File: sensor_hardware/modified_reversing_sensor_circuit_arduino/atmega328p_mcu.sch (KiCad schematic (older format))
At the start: 15 parts, among them Q1 8/16/20MHz

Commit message: mods to schematic
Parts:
- added R12, R18, R21, R24, R28: R, symbol R
- added U4: LM339, symbol LM339
- gave numbers to parts that had none: 9
- renumbered C2 to C6, C1 to C7, R2 to R32, R6 to R33, Q1 to X1
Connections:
- wire segments 59 -> 73
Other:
- note added: "Atmega328p comparator \nequivalent circuit"
- note added: "comparator electrical characteristics\ninput offset voltage @ 5V \n(conditions 0.4V < Vin <Vcc-0.5V)\n typical 10 mV, max 40 mV\ninput leakage current \n min -50 nA max 50 nA\npropogation delay\n 500 ns"

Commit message: mods to schematic
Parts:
- U1: symbol atmega328p -> atmega328p-RESCUE-reversing_sensor_circuit
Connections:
- net labels added: PosFeedback
- net labels removed: SoftCompOut
- wire segments 73 -> 71
- no-connect marks 0 -> 1
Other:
- note added: "Atmega328 only has \ninternal comp output"
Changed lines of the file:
@@
 EESchema Schematic File Version 2
+LIBS:reversing_sensor_circuit-rescue
 LIBS:power
 LIBS:device
@@
 $EndDescr
 $Comp
-L atmega328p U1
+L atmega328p-RESCUE-reversing_sensor_circuit U1
 U 1 1 61408799
 P 5650 3675
+AR Path="/61408799" Ref="U1"  Part="1"
+AR Path="/61407FAF/61408799" Ref="U1"  Part="1"
 F 0 "U1" H 5650 3375 60  0000 C CNN
 F 1 "atmega328p" H 5350 3025 60  0000 C CNN
@@
 $EndComp
 Text Label 7575 3975 2    60   ~ 0
-SoftCompOut
+PosFeedback
 $Comp
 L R R13
@@
 	8400 950  8575 950
 Connection ~ 8400 1525
-Wire Wire Line
-	9450 1625 9700 1625
-Wire Wire Line
-	9650 1625 9650 950
-Wire Wire Line
-	9650 950  8875 950
 Text Notes 8200 3550 0    60   ~ 0
 comparator electrical characteristics\ninput offset voltage @ 5V \n(conditions 0.4V < Vin <Vcc-0.5V)\n   typical 10 mV, max 40 mV\ninput leakage current           \n   min -50 nA max 50 nA\npropogation delay\n   500 ns
@@
 Wire Wire Line
 	7775 1725 7625 1725
-Text Label 9700 1625 0    60   ~ 0
-SoftCompOut
-Connection ~ 9650 1625
 Text Notes 9175 2175 0    60   ~ 0
 Atmega328p comparator \nequivalent circuit
@@
 Wire Wire Line
 	9050 1325 9050 1225
+Text Label 9100 950  0    60   ~ 0
+PosFeedback
+Wire Wire Line
+	8875 950  9100 950
+NoConn ~ 9450 1625
+Text Notes 9650 1625 0    60   ~ 0
+Atmega328 only has \ninternal comp output
 $EndSCHEMATC

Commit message: internal comparator option1, with a feedback on the positive input, but not tested yet
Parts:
- R12, R21: value R -> 8K2
- R13, R24, R25, R28: value R -> 100K
- R18, R29: value R -> 10K
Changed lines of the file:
@@
 P 8775 4075
 F 0 "R29" V 8855 4075 50  0000 C CNN
-F 1 "R" V 8775 4075 50  0000 C CNN
+F 1 "10K" V 8775 4075 50  0000 C CNN
 F 2 "" V 8705 4075 50  0001 C CNN
 F 3 "" H 8775 4075 50  0001 C CNN
@@
 P 8375 4500
 F 0 "R25" V 8455 4500 50  0000 C CNN
-F 1 "R" V 8375 4500 50  0000 C CNN
+F 1 "100K" V 8375 4500 50  0000 C CNN
 F 2 "" V 8305 4500 50  0001 C CNN
 F 3 "" H 8375 4500 50  0001 C CNN
@@
 P 7850 3975
 F 0 "R13" V 7775 3975 50  0000 C CNN
-F 1 "R" V 7850 3975 50  0000 C CNN
+F 1 "100K" V 7850 3975 50  0000 C CNN
 F 2 "" V 7780 3975 50  0001 C CNN
 F 3 "" H 7850 3975 50  0001 C CNN
@@
 P 7925 1525
 F 0 "R18" V 8005 1525 50  0000 C CNN
-F 1 "R" V 7925 1525 50  0000 C CNN
+F 1 "10K" V 7925 1525 50  0000 C CNN
 F 2 "" V 7855 1525 50  0001 C CNN
 F 3 "" H 7925 1525 50  0001 C CNN
@@
 P 8250 2025
 F 0 "R24" V 8330 2025 50  0000 C CNN
-F 1 "R" V 8250 2025 50  0000 C CNN
+F 1 "100K" V 8250 2025 50  0000 C CNN
 F 2 "" V 8180 2025 50  0001 C CNN
 F 3 "" H 8250 2025 50  0001 C CNN
@@
 P 8725 950
 F 0 "R28" V 8805 950 50  0000 C CNN
-F 1 "R" V 8725 950 50  0000 C CNN
+F 1 "100K" V 8725 950 50  0000 C CNN
 F 2 "" V 8655 950 50  0001 C CNN
 F 3 "" H 8725 950 50  0001 C CNN
@@
 P 7350 4175
 F 0 "R12" V 7430 4175 50  0000 C CNN
-F 1 "R" V 7350 4175 50  0000 C CNN
+F 1 "8K2" V 7350 4175 50  0000 C CNN
 F 2 "" V 7280 4175 50  0001 C CNN
 F 3 "" H 7350 4175 50  0001 C CNN
@@
 P 7925 1725
 F 0 "R21" V 8005 1725 50  0000 C CNN
-F 1 "R" V 7925 1725 50  0000 C CNN
+F 1 "8K2" V 7925 1725 50  0000 C CNN
 F 2 "" V 7855 1725 50  0001 C CNN
 F 3 "" H 7925 1725 50  0001 C CNN

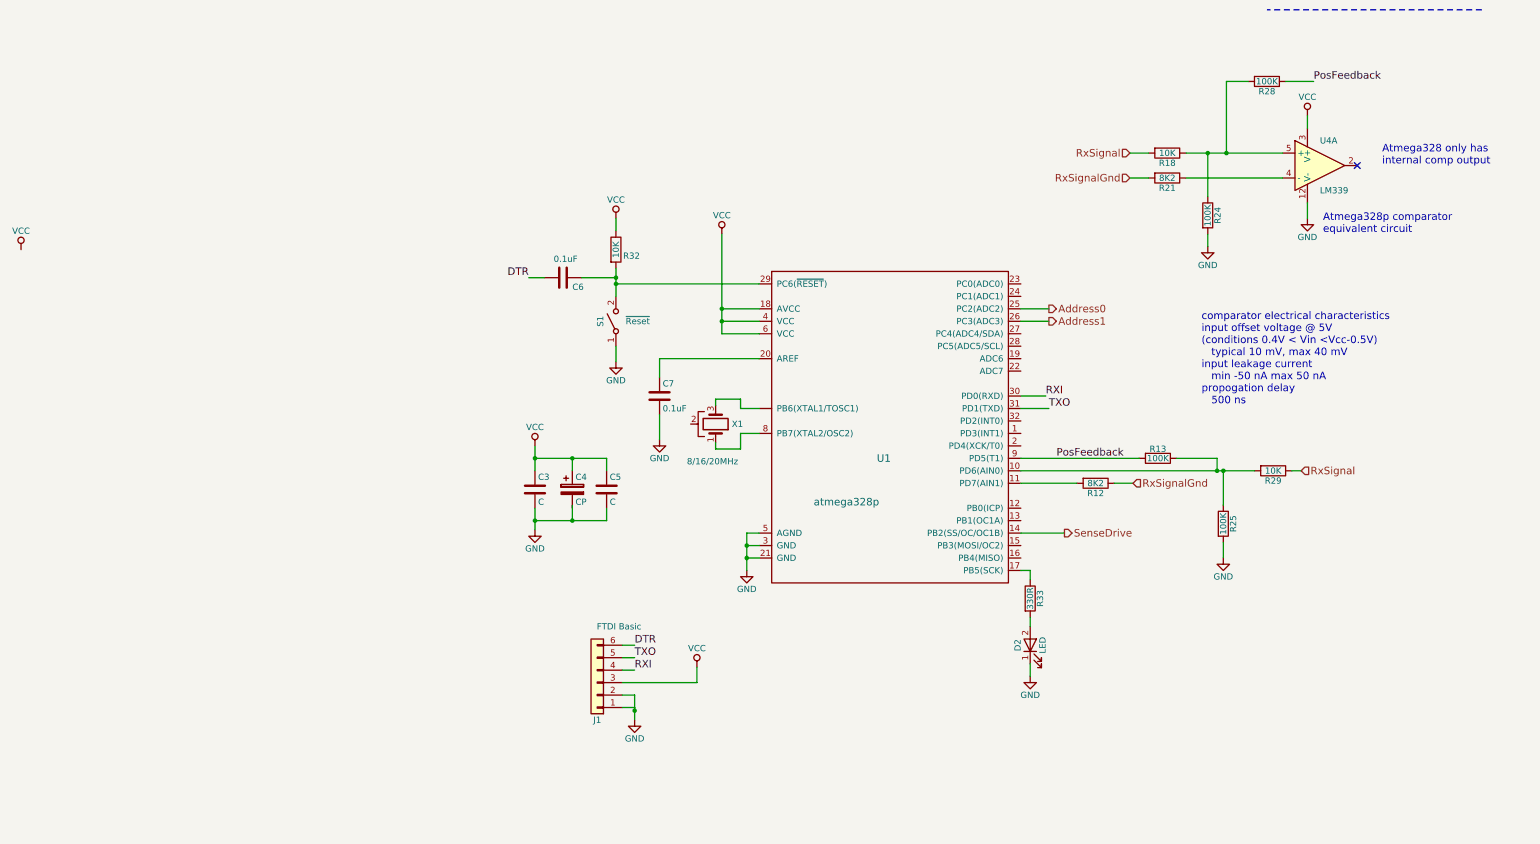
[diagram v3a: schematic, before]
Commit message: update schematic with internal comp
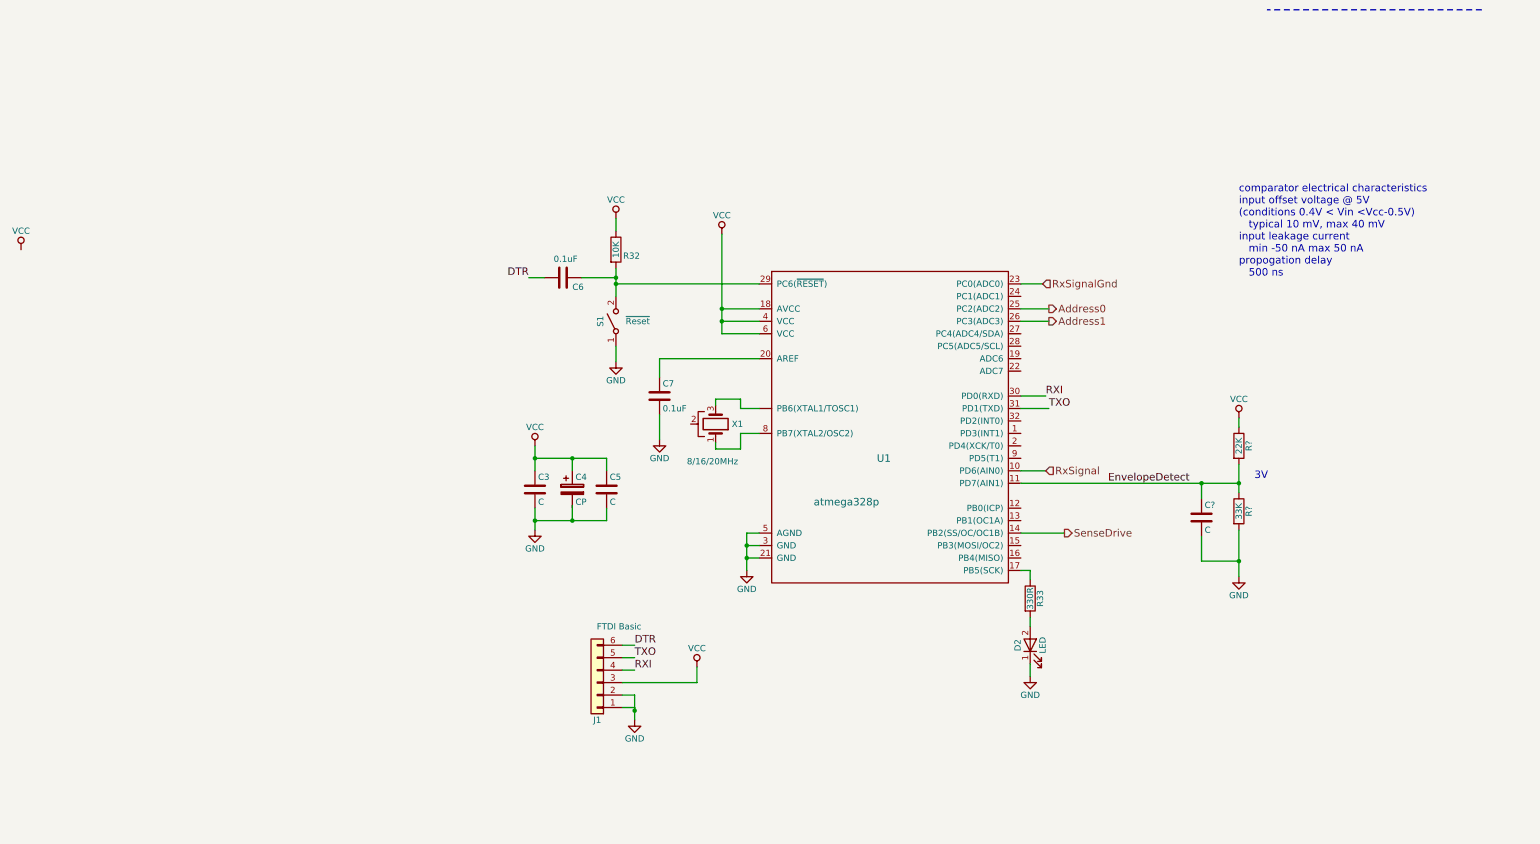
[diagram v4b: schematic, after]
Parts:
- removed R12, R21: 8K2, symbol R
- removed R13, R24, R25, R28: 100K, symbol R
- removed R18, R29: 10K, symbol R
- removed U4: LM339, symbol LM339
- added C?: C, symbol C
- added R?: 22K, symbol R
- added R?: 33K, symbol R
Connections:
- net GND: now also C?.2, R?.2
- net RxSignal: now also U1.10 (PD6(AIN0))
- net RxSignalGnd: now also U1.23 (PC0(ADC0))
- net VCC: now also R?.1
- net EnvelopeDetect: now reaches U1.11 (PD7(AIN1))
- net EnvelopeDetect: now also C?.1, R?.1, R?.2
- net PosFeedback: no longer names the net of U1.9 (PD5(T1))
- no-connect marks 1 -> 0
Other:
- note added: "3V"
- note removed: "Atmega328 only has \ninternal comp output"
- note removed: "Atmega328p comparator \nequivalent circuit"

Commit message: use polledSerial which doesnt use uart interrupts, rather than standard  Arduino.Serial
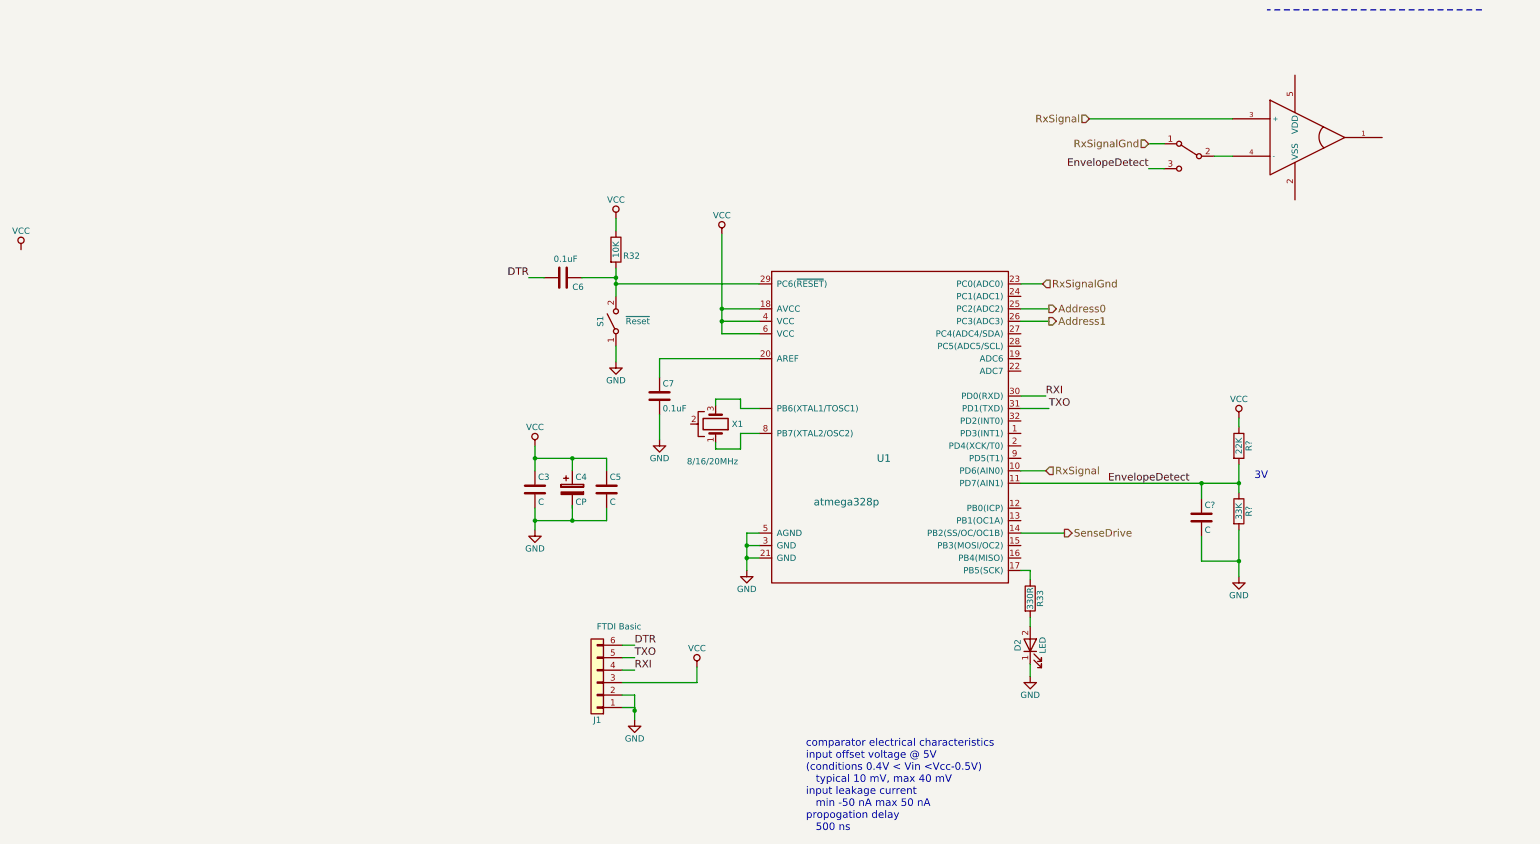
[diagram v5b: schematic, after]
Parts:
- added SW?: SW_SPDT, symbol SW_SPDT
- added U?: MCP6561, symbol MCP6561
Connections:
- net EnvelopeDetect: now also SW?.3 (C)
- net RxSignal: now also U?.3 (+)
- net RxSignalGnd: now also SW?.1 (A)
- new net: SW?.2 (B), U?.4 (-)
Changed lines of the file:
@@
 EESchema Schematic File Version 2
+LIBS:mcp6561
 LIBS:reversing_sensor_circuit-rescue
 LIBS:power
@@
 	4350 2975 4650 2975
 Wire Wire Line
-	4350 2175 4350 2775
-Wire Wire Line
-	4350 2775 4350 2875
-Wire Wire Line
-	4350 2875 4350 2975
+	4350 2175 4350 2975
 Wire Wire Line
 	4650 2775 4350 2775
@@
 	4650 4575 4550 4575
 Wire Wire Line
-	4550 4575 4550 4675
-Wire Wire Line
-	4550 4675 4550 4775
-Wire Wire Line
-	4550 4775 4550 4875
+	4550 4575 4550 4875
 Wire Wire Line
 	4650 4675 4550 4675
@@
 	3500 2150 3500 2050
 Wire Wire Line
-	3500 2450 3500 2525
-Wire Wire Line
-	3500 2525 3500 2575
-Wire Wire Line
-	3500 2575 3500 2675
+	3500 2450 3500 2675
 Wire Wire Line
 	3500 3200 3500 3075
@@
 Connection ~ 3500 2525
 Wire Wire Line
-	2850 4375 2850 4475
-Wire Wire Line
-	2850 4475 2850 4550
-Wire Wire Line
-	2850 3875 2850 3975
-Wire Wire Line
-	2850 3975 2850 4075
+	2850 4375 2850 4550
+Wire Wire Line
+	2850 3875 2850 4075
 Wire Wire Line
 	6750 4875 6825 4875
@@
 	2925 2525 2800 2525
 Wire Wire Line
-	2850 4475 3150 4475
-Wire Wire Line
-	3150 4475 3425 4475
+	2850 4475 3425 4475
 Wire Wire Line
 	3425 4475 3425 4375
@@
 Connection ~ 3150 4475
 Wire Wire Line
-	2850 3975 3150 3975
-Wire Wire Line
-	3150 3975 3425 3975
+	2850 3975 3425 3975
 Wire Wire Line
 	3425 3975 3425 4075
@@
 	3550 5875 3650 5875
 Wire Wire Line
-	3650 5875 3650 6000
-Wire Wire Line
-	3650 6000 3650 6075
+	3650 5875 3650 6075
 Wire Wire Line
 	3550 5975 3650 5975
@@
 Wire Wire Line
 	6975 3575 6750 3575
-Text Notes 8500 2525 0    60   ~ 0
+Text Notes 5025 6975 0    60   ~ 0
 comparator electrical characteristics\ninput offset voltage @ 5V \n(conditions 0.4V < Vin <Vcc-0.5V)\n   typical 10 mV, max 40 mV\ninput leakage current           \n   min -50 nA max 50 nA\npropogation delay\n   500 ns
 Wire Wire Line
@@
 $EndComp
 Wire Wire Line
-	8500 4025 8500 4175
-Wire Wire Line
-	8500 4175 8500 4250
+	8500 4025 8500 4250
 $Comp
 L GND #PWR?
@@
 $EndComp
 Wire Wire Line
-	8500 4925 8500 4800
-Wire Wire Line
-	8500 4800 8500 4550
+	8500 4550 8500 4925
 $Comp
 L VCC #PWR?
@@
 	6925 2575 6750 2575
 Wire Wire Line
-	6750 4175 8200 4175
-Wire Wire Line
-	8200 4175 8500 4175
+	6750 4175 8500 4175
 Connection ~ 8500 4175
 Text Label 7450 4175 0    60   ~ 0
@@
 	8200 4300 8200 4175
 Connection ~ 8200 4175
+$Comp
+L MCP6561 U?
+U 1 1 615ECD8F
+P 9150 1400
+F 0 "U?" H 9200 1600 60  0001 L CNN
+F 1 "MCP6561" H 9100 1200 60  0001 L CNN
+F 2 "" H 9150 1400 60  0001 C CNN
+F 3 "" H 9150 1400 60  0001 C CNN
+	1    9150 1400
+	1    0    0    -1
+$EndComp
+Text HLabel 7300 1250 0    60   Input ~ 0
+RxSignal
+Wire Wire Line
+	8450 1250 7300 1250
+Text HLabel 7775 1450 0    60   Input ~ 0
+RxSignalGnd
+Text Label 7775 1650 2    60   ~ 0
+EnvelopeDetect
+$Comp
+L SW_SPDT SW?
+U 1 1 615ED0E9
+P 8100 1550
+F 0 "SW?" H 8100 1720 50  0001 C CNN
+F 1 "SW_SPDT" H 8100 1350 50  0001 C CNN
+F 2 "" H 8100 1550 50  0001 C CNN
+F 3 "" H 8100 1550 50  0001 C CNN
+	1    8100 1550
+	-1   0    0    -1
+$EndComp
+Wire Wire Line
+	8450 1550 8300 1550
+Wire Wire Line
+	7900 1450 7775 1450
+Wire Wire Line
+	7900 1650 7775 1650
 $EndSCHEMATC

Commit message: update readme and add wifi circuit details
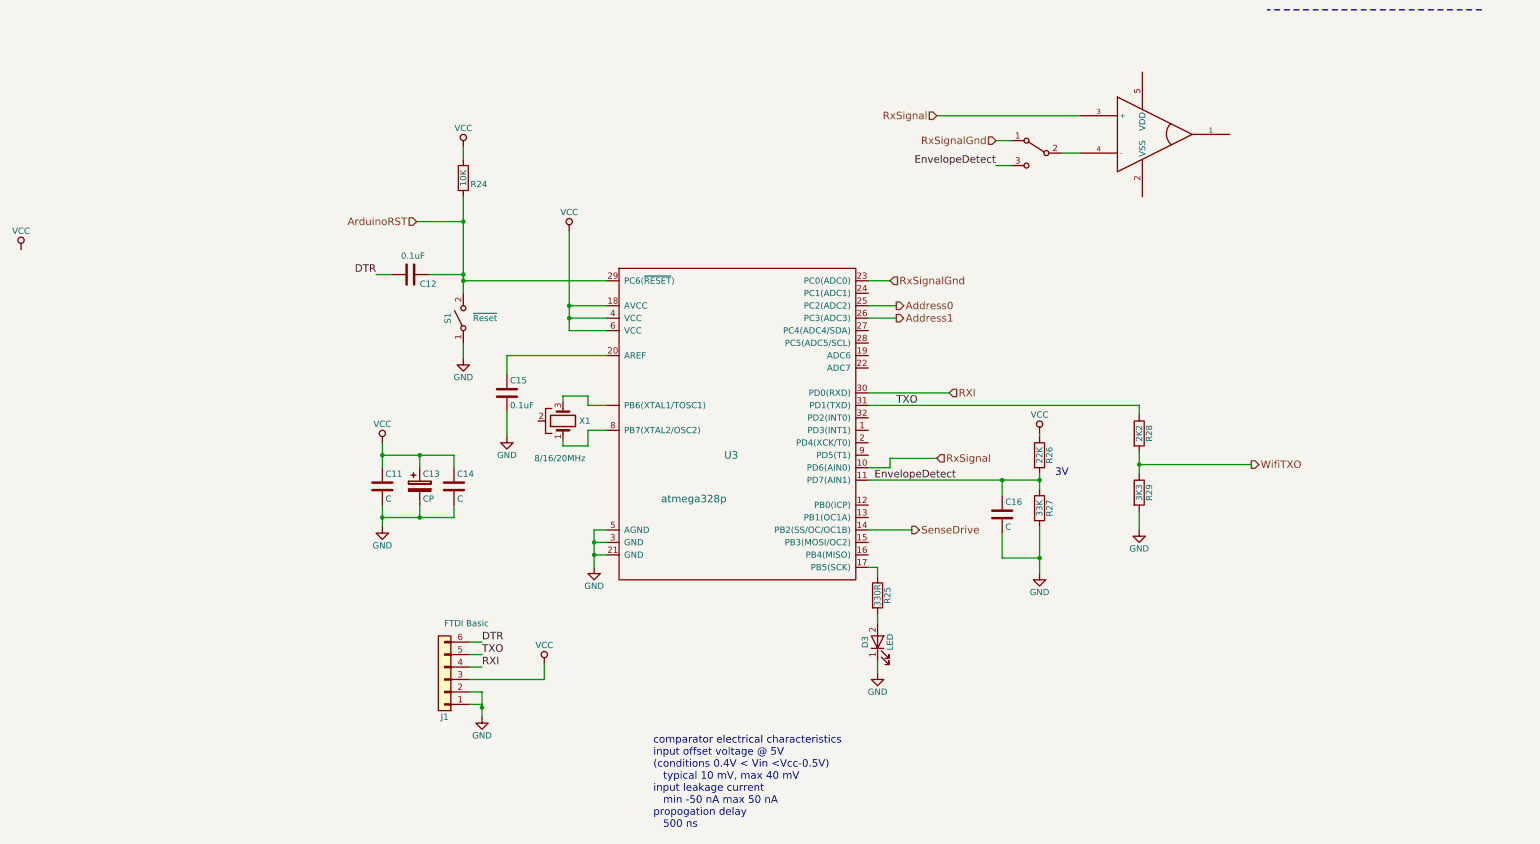
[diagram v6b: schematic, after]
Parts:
- added R28: 2K2, symbol R
- added R29: 3K3, symbol R
- gave numbers to parts that had none: 5
- renumbered C3 to C11, C6 to C12, C4 to C13, C5 to C14, C7 to C15, D2 to D3, R32 to R24, R33 to R25, U1 to U3
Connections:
- net GND: now also R29.2
- net TXO: now also R28.1
- net ArduinoRST: now reaches C12.1, R24.2, S1.2 (B), U3.29 (PC6(~RESET))
- new net WifiTXO: R28.2, R29.1
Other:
- moved on the sheet: C11, C12, C13, C14, C15, C16, D3, J1, R24, R25, R26, R27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
